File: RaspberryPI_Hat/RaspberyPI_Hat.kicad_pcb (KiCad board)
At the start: 2 copper layers, 65 x 56 mm, 45 parts, among them Q1 BC817, Q2 BC817, Q3 BC817, SW1 SW_PUSH, U1 CAT24C32WI-GT3

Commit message: Change revision number
Added separate footprint for rabbit logo

Signed-off-by: Rangel Ivanov <rangelivanov88@gmail.com>
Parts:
- removed the G*** at (117.6, 120.4)
- added G***: LOGO, myfootprint:logo, F.Cu at (107.7, 120.3)
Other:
- board text added: "RabbitMax Flex"
- board text added: "Rev 1.1 (c) 2016"
- board text added: "http://rabbitmax.com/"

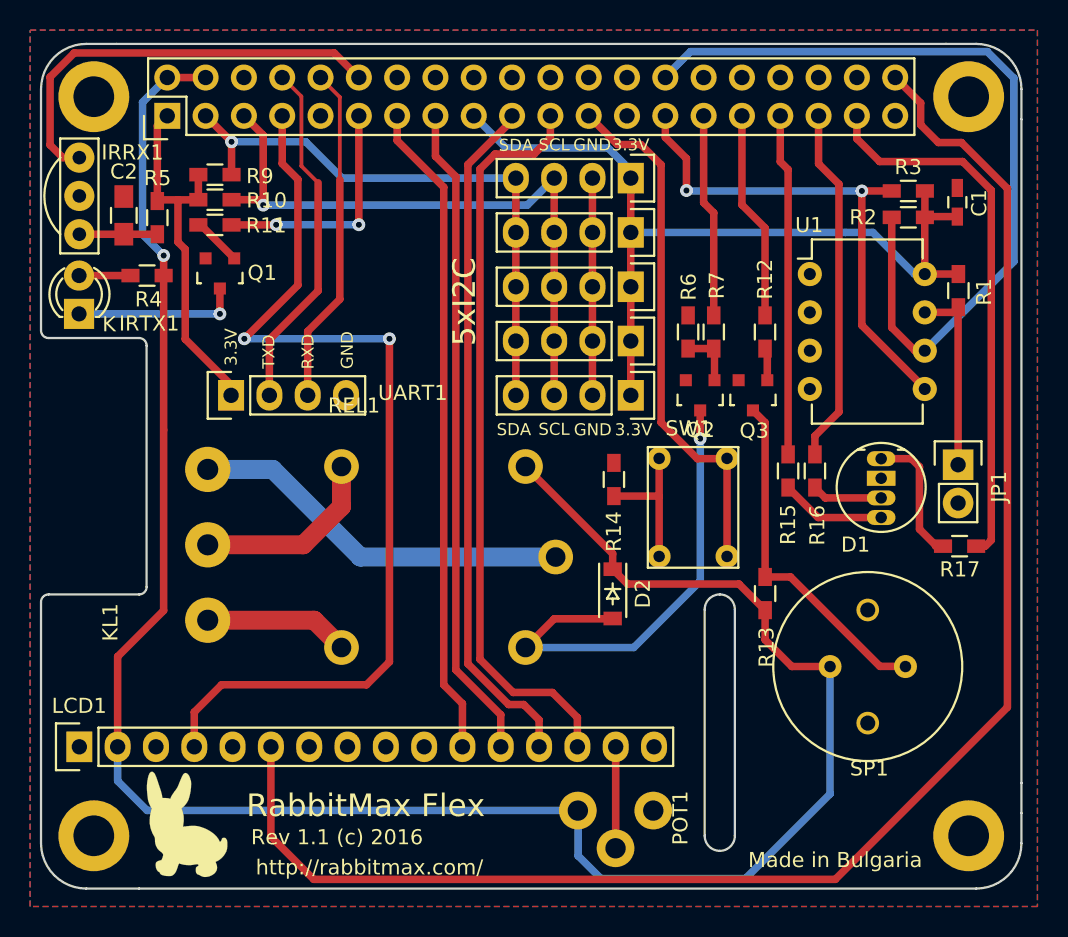
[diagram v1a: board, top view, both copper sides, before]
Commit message: RaspberyPI_Hat.kicad_pcb: Move and update labels
The following changes have been applied to the
silk screen:
- Hide labels K and KL1
- Move IRTX1
- Move REL1
- Move SW1
- Move SP1
- Center D1 under the LED
- Add EU to label "Made in Bulgaria"
- Update revision to 1.2

Signed-off-by: Leon Anavi <leon@anavi.org>
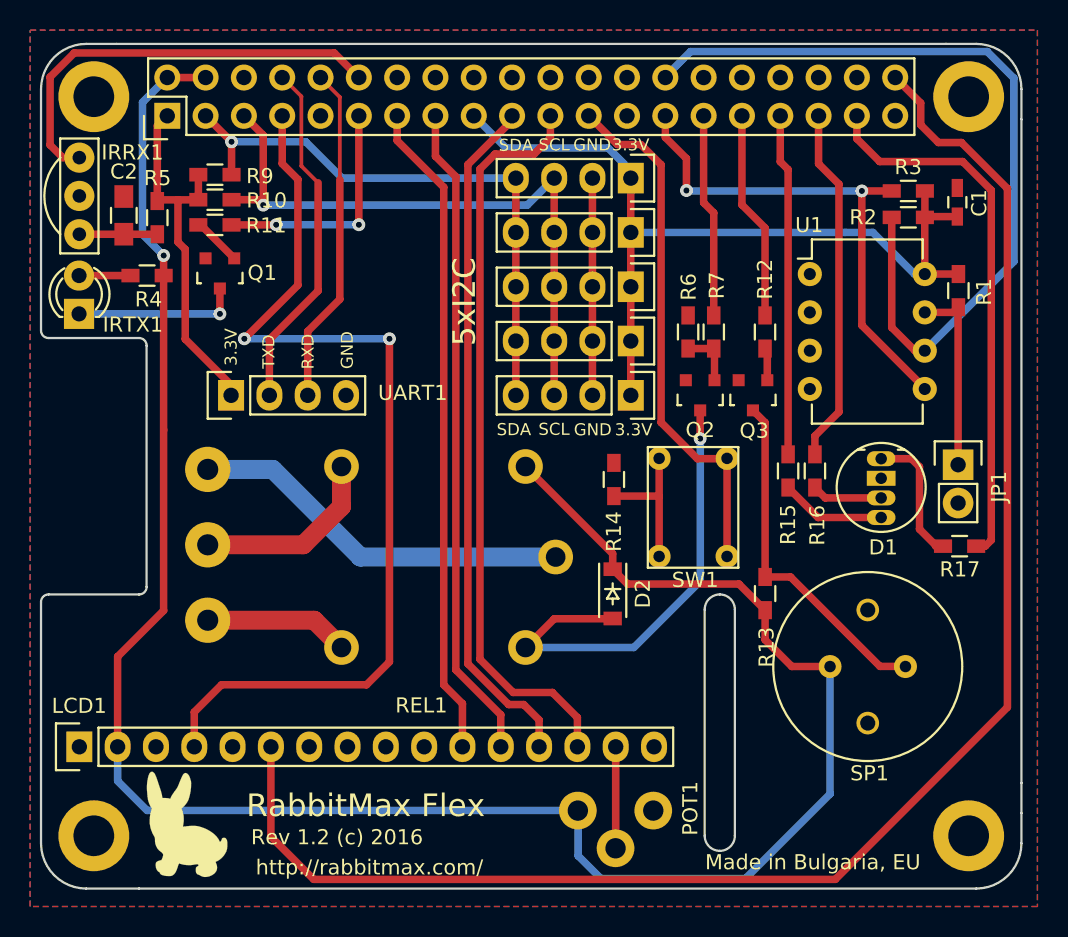
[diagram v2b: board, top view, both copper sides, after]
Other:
- board text added: "Made in Bulgaria, EU"
- board text added: "Rev 1.2 (c) 2016"
- board text removed: "Made in Bulgaria"
- board text removed: "Rev 1.1 (c) 2016"
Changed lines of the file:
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@@
-(kicad_pcb (version 4) (host pcbnew "(2016-03-19 BZR 6630)-stable")
+(kicad_pcb (version 4) (host pcbnew 4.0.2+dfsg1-stable)
   (general
     (links 111)
     (no_connects 1)
-    (area 97.924999 68.524999 163.075001 124.675001)
+    (area 86.242429 56.842428 174.757572 125.790001)
     (thickness 1.6)
     (drawings 45)
@@
       (hpglpenspeed 20)
       (hpglpendiameter 15)
+      (hpglpenoverlay 2)
       (psnegative false)
       (psa4output false)
@@
   (module myfootprint:KLEMA_1x3 (layer F.Cu)
     (at 112.55 96.81 270)
-    (fp_text reference KL1 (at 10.14 9.95 270) (layer F.SilkS)
+    (fp_text reference KL1 (at 10.14 9.95 270) (layer F.SilkS) hide
       (effects (font (size 1 1) (thickness 0.15)))
     )
@@
     (descr "5mm common cathode RGB LED")
     (tags "RGB LED 5mm Common Cathode")
-    (fp_text reference D1 (at -1.7 5.7 180) (layer F.SilkS)
+    (fp_text reference D1 (at 0.13682 5.8813 180) (layer F.SilkS)
       (effects (font (size 1 1) (thickness 0.15)))
     )
@@
     (descr "LED 3mm round vertical")
     (tags "LED  3mm round vertical")
-    (fp_text reference IRTX1 (at -0.64 4.65 180) (layer F.SilkS)
+    (fp_text reference IRTX1 (at -0.7112 3.56838 180) (layer F.SilkS)
       (effects (font (size 1 1) (thickness 0.15)))
     )
@@
     (fp_arc (start 1.311 0.034) (end 3.051 0.994) (angle 110) (layer F.SilkS) (width 0.15))
     (fp_arc (start 1.301 0.034) (end 2.335 1.094) (angle 87.5) (layer F.SilkS) (width 0.15))
-    (fp_text user K (at -0.69 1.99 180) (layer F.SilkS)
+    (fp_text user K (at -0.69 1.99 180) (layer F.SilkS) hide
       (effects (font (size 1 1) (thickness 0.15)))
     )
@@
   (module myfootprint:RAS-05-15 (layer F.Cu)
     (at 120.02 95.12)
-    (fp_text reference REL1 (at -1.27 -2.54) (layer F.SilkS)
+    (fp_text reference REL1 (at 3.19458 17.3388) (layer F.SilkS)
       (effects (font (size 1 1) (thickness 0.15)))
     )
@@
   (module myfootprint:TACT_SW_6 (layer F.Cu)
     (at 143.48 102.58 180)
-    (fp_text reference SW1 (at 2.54 8.49 180) (layer F.SilkS)
+    (fp_text reference SW1 (at 2.11458 -1.55776 180) (layer F.SilkS)
       (effects (font (size 1 1) (thickness 0.15)))
     )
@@
   (module myfootprint:MURATA_PKM13 (layer F.Cu)
     (at 150.31 109.88)
-    (fp_text reference SP1 (at 2.6 6.76) (layer F.SilkS)
+    (fp_text reference SP1 (at 2.6175 7.08222) (layer F.SilkS)
       (effects (font (size 1 1) (thickness 0.15)))
     )
@@
   (module myfootprint:POT_VERT (layer F.Cu)
     (at 133.59 119.43 90)
-    (fp_text reference POT1 (at -0.49 6.8 90) (layer F.SilkS)
+    (fp_text reference POT1 (at 0.14622 7.45538 90) (layer F.SilkS)
       (effects (font (size 1 1) (thickness 0.15)))
     )
@@
     (effects (font (size 1 1) (thickness 0.25)))
   )
-  (gr_text "Rev 1.1 (c) 2016" (at 117.625 121.2) (layer F.SilkS)
+  (gr_text "Rev 1.2 (c) 2016" (at 117.625 121.2) (layer F.SilkS)
     (effects (font (size 1 1) (thickness 0.25)))
   )
@@
     (effects (font (size 1.5 1.5) (thickness 0.3)))
   )
-  (gr_text "Made in Bulgaria" (at 150.65 122.71) (layer F.SilkS)
+  (gr_text "Made in Bulgaria, EU" (at 149.1683 122.85502) (layer F.SilkS)
     (effects (font (size 1 1) (thickness 0.15)))
   )

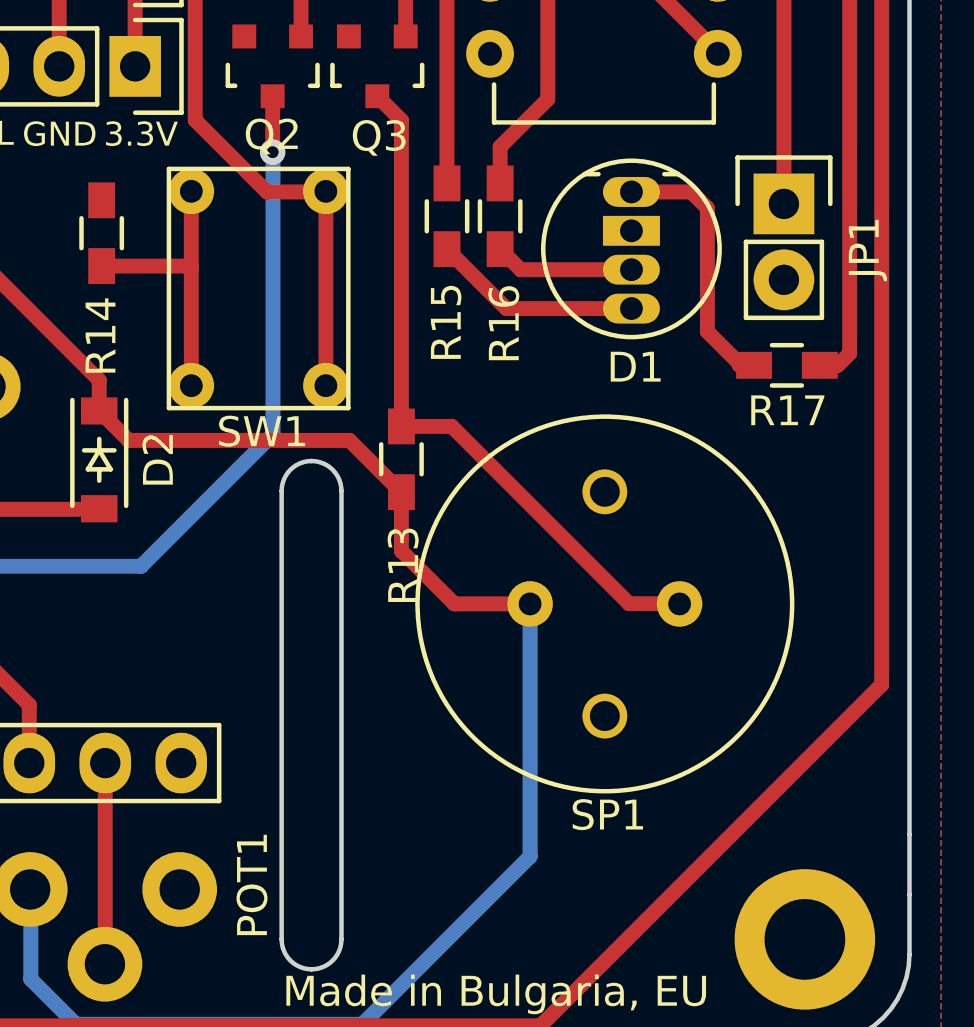
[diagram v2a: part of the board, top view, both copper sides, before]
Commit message: Changed drill sizes for button and buzzer
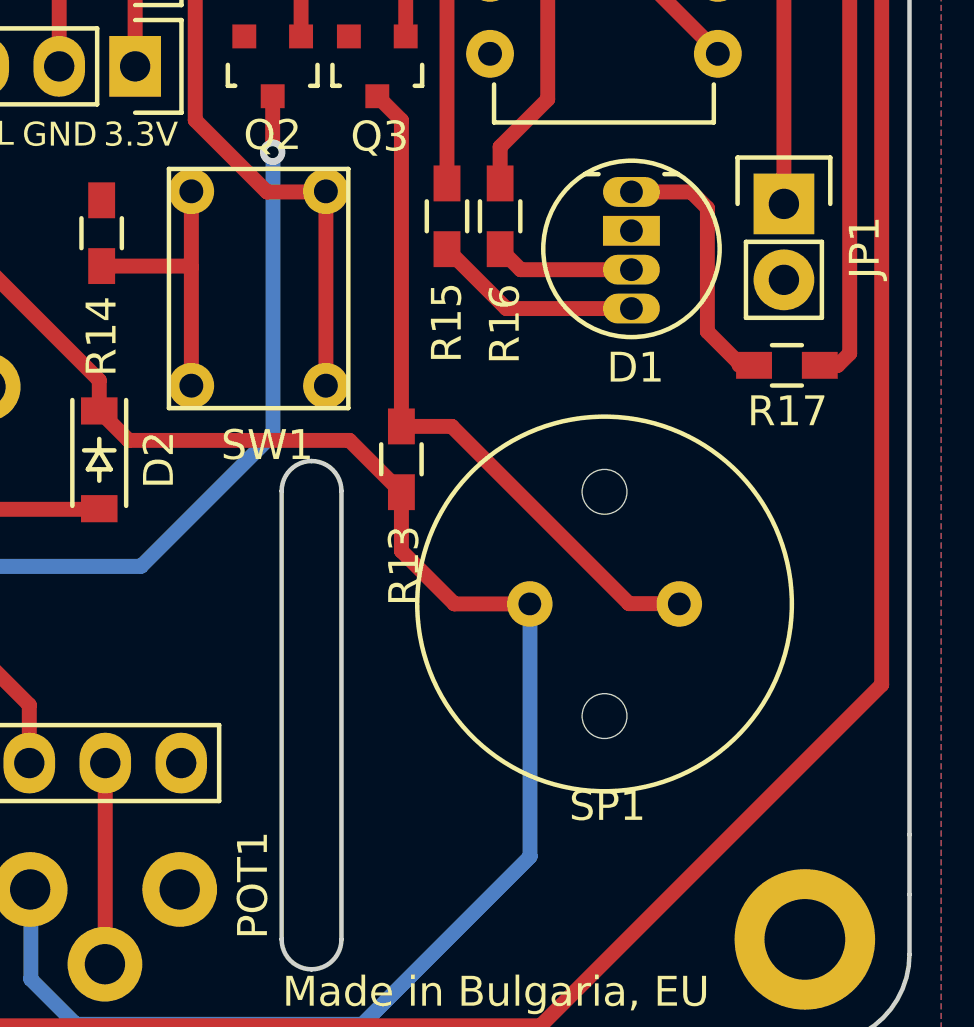
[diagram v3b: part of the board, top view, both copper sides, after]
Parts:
- moved SW1 7.91 mm to (139.0, 96.1), turned to 0 degrees
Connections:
- SW1 pad 1: Net-(RASP_CONN1-Pad23) -> Net-(R14-Pad1)
- SW1 pad 2: Net-(R14-Pad1) -> Net-(RASP_CONN1-Pad23)
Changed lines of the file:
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@@
-(kicad_pcb (version 4) (host pcbnew 4.0.2+dfsg1-stable)
+(kicad_pcb (version 4) (host pcbnew 4.0.2+e4-6225~38~ubuntu15.10.1-stable)
   (general
     (links 111)
     (no_connects 1)
-    (area 86.242429 56.842428 174.757572 125.790001)
+    (area 97.924999 68.524999 163.075001 124.675001)
     (thickness 1.6)
     (drawings 45)
@@
       (net 49 "Net-(KL1-Pad1)"))
   )
-  (module myfootprint:TACT_SW_6 (layer F.Cu)
-    (at 143.48 102.58 180)
-    (fp_text reference SW1 (at 2.11458 -1.55776 180) (layer F.SilkS)
-      (effects (font (size 1 1) (thickness 0.15)))
-    )
-    (fp_text value SW_PUSH (at 2.26 -2.29 180) (layer F.Fab)
-      (effects (font (size 1 1) (thickness 0.15)))
-    )
-    (fp_line (start -0.75 -0.75) (end 5.25 -0.75) (layer F.SilkS) (width 0.15))
-    (fp_line (start 5.25 -0.75) (end 5.25 7.25) (layer F.SilkS) (width 0.15))
-    (fp_line (start 5.25 7.25) (end -0.75 7.25) (layer F.SilkS) (width 0.15))
-    (fp_line (start -0.75 7.25) (end -0.75 -0.75) (layer F.SilkS) (width 0.15))
-    (pad 1 thru_hole circle (at 0 0 180) (size 1.524 1.524) (drill 0.762) (layers *.Cu *.Mask F.SilkS)
-      (net 29 "Net-(RASP_CONN1-Pad23)"))
-    (pad 2 thru_hole circle (at 4.5 0 180) (size 1.524 1.524) (drill 0.762) (layers *.Cu *.Mask F.SilkS)
-      (net 17 "Net-(R14-Pad1)"))
-    (pad 1 thru_hole circle (at 0 6.5 180) (size 1.524 1.524) (drill 0.762) (layers *.Cu *.Mask F.SilkS)
-      (net 29 "Net-(RASP_CONN1-Pad23)"))
-    (pad 2 thru_hole circle (at 4.5 6.5 180) (size 1.524 1.524) (drill 0.762) (layers *.Cu *.Mask F.SilkS)
-      (net 17 "Net-(R14-Pad1)"))
-  )
   (module Diodes_SMD:SOD-123 (layer F.Cu)
     (at 135.9 105.06 270)
@@
     (pad 2 smd rect (at 1.635 0 270) (size 0.91 1.22) (layers F.Cu F.Paste F.Mask)
       (net 5 "Net-(D2-Pad2)"))
-  )
-  (module myfootprint:MURATA_PKM13 (layer F.Cu)
-    (at 150.31 109.88)
-    (fp_text reference SP1 (at 2.6175 7.08222) (layer F.SilkS)
-      (effects (font (size 1 1) (thickness 0.15)))
-    )
-    (fp_text value MCKPI-G1410-3668 (at 3 -7.25) (layer F.Fab)
-      (effects (font (size 1 1) (thickness 0.15)))
-    )
-    (fp_circle (center 2.5 0) (end 5.5 5.5) (layer F.SilkS) (width 0.15))
-    (pad 1 thru_hole circle (at 0 0) (size 1.524 1.524) (drill 0.762) (layers *.Cu *.Mask F.SilkS)
-      (net 4 +5V))
-    (pad 2 thru_hole circle (at 5 0) (size 1.524 1.524) (drill 0.762) (layers *.Cu *.Mask F.SilkS)
-      (net 16 "Net-(Q3-Pad3)"))
-    (pad "" np_thru_hole circle (at 2.5 -3.75) (size 1.5 1.5) (drill 1) (layers *.Cu *.Mask F.SilkS))
-    (pad "" np_thru_hole circle (at 2.5 3.75) (size 1.5 1.5) (drill 1) (layers *.Cu *.Mask F.SilkS))
   )
   (module myfootprint:POT_VERT (layer F.Cu)
@@
       (xy -2.418658 -3.439868) (xy -2.366727 -3.483398) (xy -2.310234 -3.499233) (xy -2.249089 -3.487442)) (layer F.SilkS) (width 0.01))
   )
+  (module myfootprint:TACT_SW_6 (layer F.Cu)
+    (at 138.98 96.08)
+    (fp_text reference SW1 (at 2.54 8.49) (layer F.SilkS)
+      (effects (font (size 1 1) (thickness 0.15)))
+    )
+    (fp_text value SW_PUSH (at 2.26 -2.29) (layer F.Fab)
+      (effects (font (size 1 1) (thickness 0.15)))
+    )
+    (fp_line (start -0.75 -0.75) (end 5.25 -0.75) (layer F.SilkS) (width 0.15))
+    (fp_line (start 5.25 -0.75) (end 5.25 7.25) (layer F.SilkS) (width 0.15))
+    (fp_line (start 5.25 7.25) (end -0.75 7.25) (layer F.SilkS) (width 0.15))
+    (fp_line (start -0.75 7.25) (end -0.75 -0.75) (layer F.SilkS) (width 0.15))
+    (pad 1 thru_hole circle (at 0 0) (size 1.524 1.524) (drill 0.8) (layers *.Cu *.Mask F.SilkS)
+      (net 17 "Net-(R14-Pad1)"))
+    (pad 2 thru_hole circle (at 4.5 0) (size 1.524 1.524) (drill 0.8) (layers *.Cu *.Mask F.SilkS)
+      (net 29 "Net-(RASP_CONN1-Pad23)"))
+    (pad 1 thru_hole circle (at 0 6.5) (size 1.524 1.524) (drill 0.8) (layers *.Cu *.Mask F.SilkS)
+      (net 17 "Net-(R14-Pad1)"))
+    (pad 2 thru_hole circle (at 4.5 6.5) (size 1.524 1.524) (drill 0.8) (layers *.Cu *.Mask F.SilkS)
+      (net 29 "Net-(RASP_CONN1-Pad23)"))
+  )
+  (module myfootprint:MURATA_PKM13 (layer F.Cu)
+    (at 150.3 109.88)
+    (fp_text reference SP1 (at 2.6 6.76) (layer F.SilkS)
+      (effects (font (size 1 1) (thickness 0.15)))
+    )
+    (fp_text value MCKPI-G1410-3668 (at 3 -7.25) (layer F.Fab)
+      (effects (font (size 1 1) (thickness 0.15)))
+    )
+    (fp_circle (center 2.5 0) (end 5.5 5.5) (layer F.SilkS) (width 0.15))
+    (pad 1 thru_hole circle (at 0 0) (size 1.524 1.524) (drill 0.762) (layers *.Cu *.Mask F.SilkS)
+      (net 4 +5V))
+    (pad 2 thru_hole circle (at 5 0) (size 1.524 1.524) (drill 0.762) (layers *.Cu *.Mask F.SilkS)
+      (net 16 "Net-(Q3-Pad3)"))
+    (pad "" np_thru_hole circle (at 2.5 -3.75) (size 1.5 1.5) (drill 1.5) (layers *.Cu *.Mask F.SilkS))
+    (pad "" np_thru_hole circle (at 2.5 3.75) (size 1.5 1.5) (drill 1.5) (layers *.Cu *.Mask F.SilkS))
+  )
   (gr_text http://rabbitmax.com/ (at 119.775 123.2) (layer F.SilkS)
